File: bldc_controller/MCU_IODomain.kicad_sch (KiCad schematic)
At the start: 7 parts

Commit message: added IPC-7351 compliant footprints and started routing
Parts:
- C67, C68, C69: footprint Capacitor_SMD:C_0402_1005Metric -> 0_capacitor_smd:C_0402_1005_DensityHigh
- R3, R4, R5: footprint Resistor_SMD:R_0402_1005Metric -> 0_resistor_smd:R_0402_1005_DensityHigh
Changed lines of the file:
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@@
       (effects (font (size 1.27 1.27)) (justify left))
     )
-    (property "Footprint" "Capacitor_SMD:C_0402_1005Metric" (at 138.43 130.81 0)
+    (property "Footprint" "0_capacitor_smd:C_0402_1005_DensityHigh" (at 138.43 130.81 0)
       (effects (font (size 1.27 1.27)) hide)
     )
@@
       (effects (font (size 1.27 1.27)))
     )
-    (property "Footprint" "Resistor_SMD:R_0402_1005Metric" (at 153.67 121.92 0)
+    (property "Footprint" "0_resistor_smd:R_0402_1005_DensityHigh" (at 153.67 121.92 0)
       (effects (font (size 1.27 1.27)) hide)
     )
@@
       (effects (font (size 1.27 1.27)) (justify left))
     )
-    (property "Footprint" "Capacitor_SMD:C_0402_1005Metric" (at 143.51 130.81 0)
+    (property "Footprint" "0_capacitor_smd:C_0402_1005_DensityHigh" (at 143.51 130.81 0)
       (effects (font (size 1.27 1.27)) hide)
     )
@@
       (effects (font (size 1.27 1.27)))
     )
-    (property "Footprint" "Resistor_SMD:R_0402_1005Metric" (at 153.67 124.46 0)
+    (property "Footprint" "0_resistor_smd:R_0402_1005_DensityHigh" (at 153.67 124.46 0)
       (effects (font (size 1.27 1.27)) hide)
     )
@@
       (effects (font (size 1.27 1.27)) (justify left))
     )
-    (property "Footprint" "Capacitor_SMD:C_0402_1005Metric" (at 148.59 130.81 0)
+    (property "Footprint" "0_capacitor_smd:C_0402_1005_DensityHigh" (at 148.59 130.81 0)
       (effects (font (size 1.27 1.27)) hide)
     )
@@
       (effects (font (size 1.27 1.27)))
     )
-    (property "Footprint" "Resistor_SMD:R_0402_1005Metric" (at 153.67 127 0)
+    (property "Footprint" "0_resistor_smd:R_0402_1005_DensityHigh" (at 153.67 127 0)
       (effects (font (size 1.27 1.27)) hide)
     )

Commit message: some progress on the pcb
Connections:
- net PWM_PHASEA: now also U?.10 (PA2); no longer U?.8 (PA0)
- net PWM_PHASEC: now also U?.8 (PA0); no longer U?.10 (PA2)
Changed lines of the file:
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@@
     (effects (font (size 1.27 1.27)) (justify right bottom))
   )
-  (label "PWM_PHASEC" (at 82.55 41.91 0) (fields_autoplaced)
+  (label "PWM_PHASEC" (at 82.55 36.83 0) (fields_autoplaced)
     (effects (font (size 1.27 1.27)) (justify left bottom))
   )
@@
     (effects (font (size 1.27 1.27)) (justify left bottom))
   )
-  (label "PWM_PHASEA" (at 82.55 36.83 0) (fields_autoplaced)
-    (effects (font (size 1.27 1.27)) (justify left bottom))
-  )
+  (label "PWM_PHASEA" (at 82.55 41.91 0) (fields_autoplaced)
+    (effects (font (size 1.27 1.27)) (justify left bottom))
+  )

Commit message: added power domains. Risk of ground shift near CAN
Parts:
- removed U?: STM32G474CEUx, Package_DFN_QFN:QFN-48-1EP_7x7mm_P0.5mm_EP5.6x5.6mm, symbol 0_mcu:STM32G474CEUx
- added U5: STM32G474RET3, Package_QFP:LQFP-64_10x10mm_P0.5mm, symbol 0_mcu:STM32G474RETx
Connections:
- net AUX1_A: now also U5.19 (PA5), U5.36 (PB14)
- net AUX1_B: now also U5.57 (PB4)
- net AUX1_C: now also U5.21 (PA7)
- net AUX1_D: now also U5.51 (PA15)
- net AUX1_E: now also U5.56 (PB3), U5.62 (PB9)
- net AUX1_I2C_PULLUP: now also U5.61 (PB8)
- net AUX2_A: now also U5.6 (PF1)
- net AUX2_B: now also U5.44 (PA10), U5.5 (PF0)
- net AUX2_C: now also U5.22 (PC4), U5.45 (PA11)
- net AUX2_D: now also U5.60 (PB7)
- net AUX2_I2C_PULLUP: now also U5.46 (PA12)
- net BOARD_VERSION: now also U5.18 (PA4)
- net DRV_CS: now also U5.24 (PB0)
- net DRV_MISO: now also U5.53 (PC11)
- net DRV_MOSI: now also U5.2 (PC13)
- net DRV_SCLK: now also U5.52 (PC10)
- net FDCAN_RX: now also U5.58 (PB5)
- net FDCAN_TX: now also U5.59 (PB6)
- net FILTER_SOA: now also U5.17 (PA3)
- net FILTER_SOB: now also U5.20 (PA6)
- net FILTER_SOC: now also U5.25 (PB1)
- net LED1: now also U5.37 (PB15)
- net LED2: now also U5.38 (PC6)
- net MOTOR_ENABLE: now also U5.3 (PC14)
- net MOTOR_FAULT: now also U5.35 (PB13)
- net MOTOR_HIZ: now also U5.4 (PC15)
- net NRST: now also U5.7 (PG10)
- net POS_SENSOR_CS: now also U5.26 (PB2)
- net PWM_PHASEA: now also U5.14 (PA2)
- net PWM_PHASEB: now also U5.13 (PA1)
- net PWM_PHASEC: now also U5.12 (PA0)
- net RS422_DE: now also U5.33 (PB11)
- net RS422_~{RE}: now also U5.30 (PB10)
- net SENSE_TEMP_FET: now also U5.34 (PB12)
- net SENSE_TEMP_MOT: now also U5.42 (PA8)
- net SENSE_VBAT: now also U5.43 (PA9)
- net SWCLK: now also U5.50 (PA14)
- net SWDIO: now also U5.49 (PA13)
- new net FAN_CTRL: U5.55 (PD2)
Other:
- moved on the sheet: C67, C68, C69, R3, R4, R5

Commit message: might have fixed net issue, added dxf and svgs
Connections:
- net PC1: now reaches U5.10 (PC2)
- net PC1: now also U5.9 (PC1)
- net PC3: now reaches U5.11 (PC3)
- net PC5: now reaches U5.23 (PC5)
- net PC7: now reaches U5.39 (PC7)
- net PC8: now reaches U5.40 (PC8)
- net PC9: now reaches U5.41 (PC9)
- net PC12: now reaches U5.54 (PC12)
- net PC0: now reaches U5.8 (PC0)
- no-connect marks 0 -> 9
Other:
- note removed: "Reference:"
- moved on the sheet: C67, C68, C69, R3, R4, R5, U5B

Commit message: starting rerouting for PCBWay 8/8 mils, 0.25mm drill
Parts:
- U5: footprint Package_QFP:LQFP-64_10x10mm_P0.5mm -> 0_package_QFP:LQFP-64_10x10mm_P0.5mm
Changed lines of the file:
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@@
       (effects (font (size 1.27 1.27)))
     )
-    (property "Footprint" "Package_QFP:LQFP-64_10x10mm_P0.5mm" (at 138.43 180.34 0)
+    (property "Footprint" "0_package_QFP:LQFP-64_10x10mm_P0.5mm" (at 138.43 180.34 0)
       (effects (font (size 1.27 1.27)) (justify right) hide)
     )

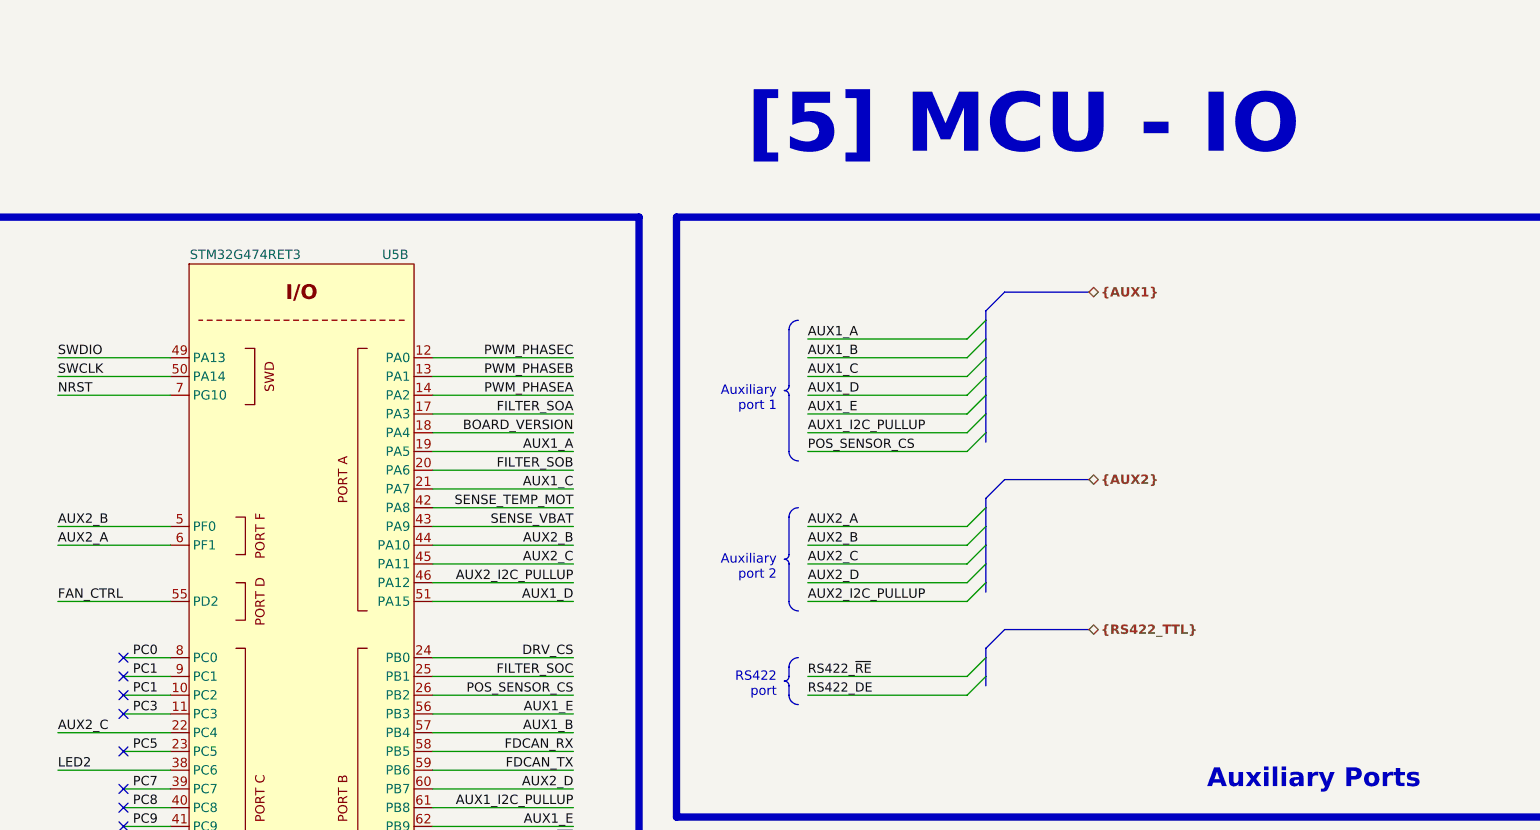
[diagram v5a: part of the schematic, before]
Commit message: Replaced 3v3 buck with WSON package alternative. Will back-annotate components
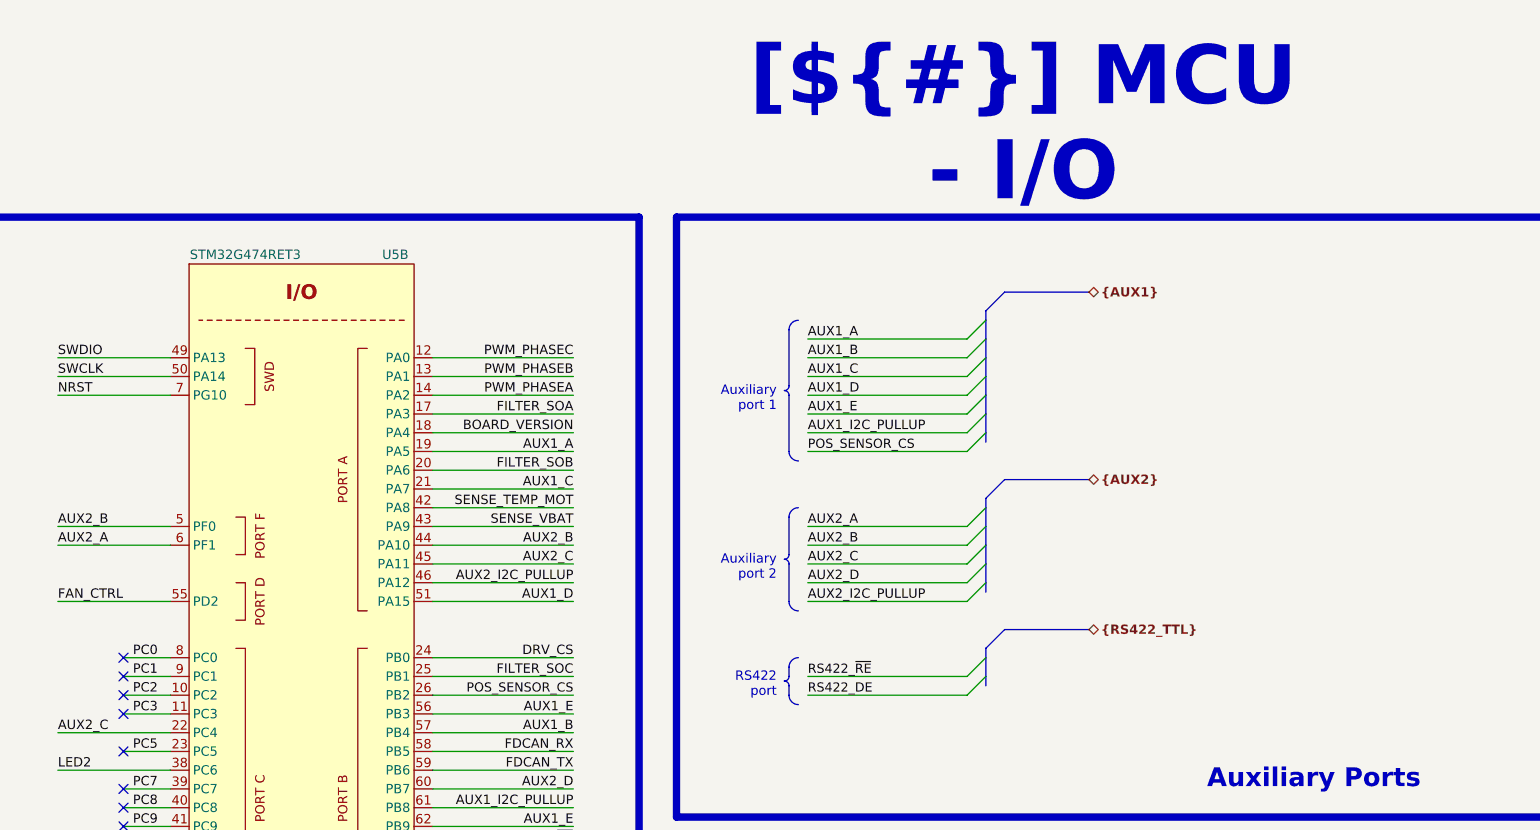
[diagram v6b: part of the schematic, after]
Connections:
- net PC1: no longer U5.10 (PC2)
- new net PC2: U5.10 (PC2)
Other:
- company: EPFL Xplore -> ${COMPANY}
- title: STM32G474 I/O Domain -> MCU - I/O
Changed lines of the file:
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@@
   (paper "A3")
   (title_block
-    (title "STM32G474 I/O Domain")
+    (title "MCU - I/O")
     (date "2023-10-14")
-    (rev "1.0")
-    (company "EPFL Xplore")
-    (comment 3 "Author: Vincent Nguyen")
+    (rev "${REVISION}")
+    (company "${COMPANY}")
+    (comment 3 "Author: ${AUTHOR}")
   )
   (junction (at 193.04 177.8) (diameter 0) (color 0 0 0 0)
@@
     (effects (font (size 1.27 1.27)) (justify right top))
   )
-  (text_box "[5] MCU - IO"
+  (text_box "[${#}] ${TITLE}"
     (at 161.29 20.32 0) (size 96.52 12.7)
     (stroke (width -0.0001) (type default))
@@
     (effects (font (size 1.27 1.27)) (justify left bottom))
   )
-  (label "PC1" (at 88.9 104.14 0) (fields_autoplaced)
+  (label "PC2" (at 88.9 104.14 0) (fields_autoplaced)
     (effects (font (size 1.27 1.27)) (justify left bottom))
   )
